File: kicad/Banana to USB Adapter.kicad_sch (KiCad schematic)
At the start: 8 parts, among them J1 USB_A, J2 Positive, J3 Negative, J4 Data

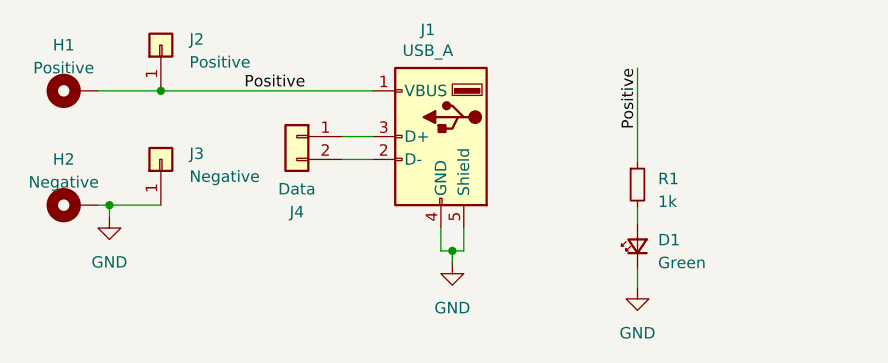
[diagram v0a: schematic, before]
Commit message: rev2 addresses #2, #3, #5, #6, #7
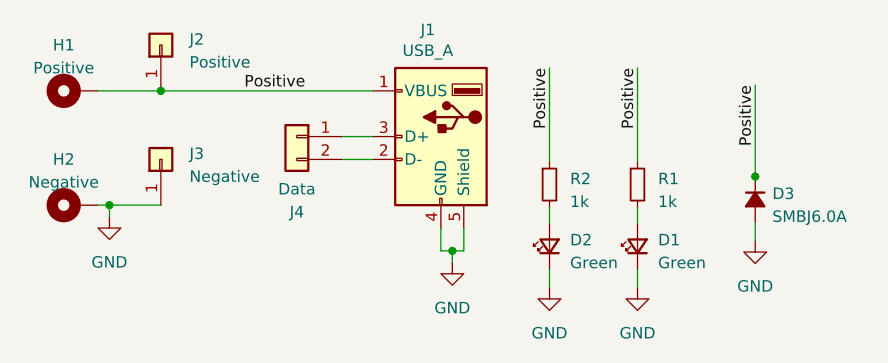
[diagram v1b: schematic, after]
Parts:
- added D2: Green, LED_SMD:LED_1206_3216Metric_Pad1.42x1.75mm_HandSolder, symbol Device:LED_Small
- added D3: SMBJ6.0A, Diode_SMD:D_SMA-SMB_Universal_Handsoldering, symbol Device:D_Small_Filled
- added R2: 1k, Resistor_SMD:R_1206_3216Metric_Pad1.30x1.75mm_HandSolder, symbol Device:R_Small
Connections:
- net GND: now also D2.1 (K), D3.2 (A)
- net Positive: now also D3.1 (K), R2.1
- new net: D2.2 (A), R2.2
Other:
- company: (none) -> baldengineer.com
- title: (none) -> Banana-to-usb adapter
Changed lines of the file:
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@@
-(kicad_sch (version 20221206) (generator eeschema)
+(kicad_sch (version 20230121) (generator eeschema)
   (paper "A4")
+  (title_block
+    (title "Banana-to-usb adapter")
+    (rev "2")
+    (company "baldengineer.com")
+  )
+  (junction (at 241.935 86.995) (diameter 0) (color 0 0 0 0)
+  )
   (junction (at 208.28 95.25) (diameter 0) (color 0 0 0 0)
   )
@@
     (stroke (width 0) (type default))
   )
+  (wire (pts (xy 241.935 76.835) (xy 241.935 86.995))
+    (stroke (width 0) (type default))
+  )
   (wire (pts (xy 168.91 77.47) (xy 175.895 77.47))
     (stroke (width 0) (type default))
@@
     (stroke (width 0) (type default))
   )
+  (wire (pts (xy 219.075 97.282) (xy 219.075 99.314))
+    (stroke (width 0) (type default))
+  )
   (wire (pts (xy 196.088 85.09) (xy 199.39 85.09))
     (stroke (width 0) (type default))
@@
     (stroke (width 0) (type default))
   )
+  (wire (pts (xy 241.935 86.995) (xy 241.935 87.249))
+    (stroke (width 0) (type default))
+  )
   (wire (pts (xy 175.895 77.47) (xy 199.39 77.47))
     (stroke (width 0) (type default))
   )
+  (wire (pts (xy 241.935 92.075) (xy 241.935 94.107))
+    (stroke (width 0) (type default))
+  )
   (wire (pts (xy 209.55 95.25) (xy 209.55 92.71))
     (stroke (width 0) (type default))
@@
   )
   (wire (pts (xy 207.01 95.25) (xy 208.28 95.25))
+    (stroke (width 0) (type default))
+  )
+  (wire (pts (xy 219.075 74.93) (xy 219.075 85.344))
+    (stroke (width 0) (type default))
+  )
+  (wire (pts (xy 219.075 90.424) (xy 219.075 92.202))
     (stroke (width 0) (type default))
   )
@@
     )
   )
+  (label "Positive" (at 219.075 74.93 270) (fields_autoplaced)
+    (effects (font (size 1.27 1.27)) (justify right bottom))
+    (property "Netclass" "Power" (at 220.345 74.93 90)
+      (effects (font (size 1.27 1.27) italic) (justify right) hide)
+    )
+  )
+  (label "Positive" (at 241.935 76.835 270) (fields_autoplaced)
+    (effects (font (size 1.27 1.27)) (justify right bottom))
+    (property "Netclass" "Power" (at 243.205 76.835 90)
+      (effects (font (size 1.27 1.27) italic) (justify right) hide)
+    )
+  )
   (symbol (lib_id "Mechanical:MountingHole_Pad") (at 166.37 90.17 90) (unit 1)
     (in_bom yes) (on_board yes) (dnp no) (fields_autoplaced)
@@
         (path "/b8d30d27-a840-4da1-9b57-1f9fe5fa1469"
           (reference "#PWR02") (unit 1)
+        )
+      )
+    )
+  )
+  (symbol (lib_id "Device:LED_Small") (at 219.075 94.742 90) (unit 1)
+    (in_bom yes) (on_board yes) (dnp no) (fields_autoplaced)
+    (property "Reference" "D2" (at 221.361 94.0435 90)
+      (effects (font (size 1.27 1.27)) (justify right))
+    )
+    (property "Value" "Green" (at 221.361 96.5835 90)
+      (effects (font (size 1.27 1.27)) (justify right))
+    )
+    (property "Footprint" "LED_SMD:LED_1206_3216Metric_Pad1.42x1.75mm_HandSolder" (at 219.075 94.742 90)
+      (effects (font (size 1.27 1.27)) hide)
+    )
+    (property "Datasheet" "~" (at 219.075 94.742 90)
+      (effects (font (size 1.27 1.27)) hide)
+    )
+    (pin "1")
+    (pin "2")
+    (instances
+      (project "Banana to USB Adapter"
+        (path "/b8d30d27-a840-4da1-9b57-1f9fe5fa1469"
+          (reference "D2") (unit 1)
         )
       )
@@
     )
   )
+  (symbol (lib_id "power:GND") (at 219.075 99.314 0) (unit 1)
+    (in_bom yes) (on_board yes) (dnp no) (fields_autoplaced)
+    (property "Reference" "#PWR05" (at 219.075 105.664 0)
+      (effects (font (size 1.27 1.27)) hide)
+    )
+    (property "Value" "GND" (at 219.075 104.394 0)
+      (effects (font (size 1.27 1.27)))
+    )
+    (property "Footprint" "" (at 219.075 99.314 0)
+      (effects (font (size 1.27 1.27)) hide)
+    )
+    (property "Datasheet" "" (at 219.075 99.314 0)
+      (effects (font (size 1.27 1.27)) hide)
+    )
+    (pin "1")
+    (instances
+      (project "Banana to USB Adapter"
+        (path "/b8d30d27-a840-4da1-9b57-1f9fe5fa1469"
+          (reference "#PWR05") (unit 1)
+        )
+      )
+    )
+  )
   (symbol (lib_id "Connector_Generic:Conn_01x01") (at 175.895 85.09 90) (unit 1)
     (in_bom yes) (on_board yes) (dnp no) (fields_autoplaced)
@@
         (path "/b8d30d27-a840-4da1-9b57-1f9fe5fa1469"
           (reference "J3") (unit 1)
+        )
+      )
+    )
+  )
+  (symbol (lib_id "Device:D_Small_Filled") (at 241.935 89.535 270) (unit 1)
+    (in_bom yes) (on_board yes) (dnp no) (fields_autoplaced)
+    (property "Reference" "D3" (at 243.84 88.9 90)
+      (effects (font (size 1.27 1.27)) (justify left))
+    )
+    (property "Value" "SMBJ6.0A" (at 243.84 91.44 90)
+      (effects (font (size 1.27 1.27)) (justify left))
+    )
+    (property "Footprint" "Diode_SMD:D_SMA-SMB_Universal_Handsoldering" (at 241.935 89.535 90)
+      (effects (font (size 1.27 1.27)) hide)
+    )
+    (property "Datasheet" "https://www.farnell.com/datasheets/1874873.pdf" (at 241.935 89.535 90)
+      (effects (font (size 1.27 1.27)) hide)
+    )
+    (property "Sim.Device" "D" (at 241.935 89.535 0)
+      (effects (font (size 1.27 1.27)) hide)
+    )
+    (property "Sim.Pins" "1=K 2=A" (at 241.935 89.535 0)
+      (effects (font (size 1.27 1.27)) hide)
+    )
+    (pin "1")
+    (pin "2")
+    (instances
+      (project "Banana to USB Adapter"
+        (path "/b8d30d27-a840-4da1-9b57-1f9fe5fa1469"
+          (reference "D3") (unit 1)
         )
       )
@@
         )
       )
+    )
+  )
+  (symbol (lib_id "power:GND") (at 241.935 94.107 0) (unit 1)
+    (in_bom yes) (on_board yes) (dnp no) (fields_autoplaced)
+    (property "Reference" "#PWR04" (at 241.935 100.457 0)
+      (effects (font (size 1.27 1.27)) hide)
+    )
+    (property "Value" "GND" (at 241.935 99.187 0)
+      (effects (font (size 1.27 1.27)))
+    )
+    (property "Footprint" "" (at 241.935 94.107 0)
+      (effects (font (size 1.27 1.27)) hide)
+    )
+    (property "Datasheet" "" (at 241.935 94.107 0)
+      (effects (font (size 1.27 1.27)) hide)
+    )
+    (pin "1")
+    (instances
+      (project "Banana to USB Adapter"
+        (path "/b8d30d27-a840-4da1-9b57-1f9fe5fa1469"
+          (reference "#PWR04") (unit 1)
+        )
+      )
+    )
+  )
+  (symbol (lib_id "Device:R_Small") (at 219.075 87.884 0) (unit 1)
+    (in_bom yes) (on_board yes) (dnp no) (fields_autoplaced)
+    (property "Reference" "R2" (at 221.361 87.249 0)
+      (effects (font (size 1.27 1.27)) (justify left))
+    )
+    (property "Value" "1k" (at 221.361 89.789 0)
+      (effects (font (size 1.27 1.27)) (justify left))
+    )
+    (property "Footprint" "Resistor_SMD:R_1206_3216Metric_Pad1.30x1.75mm_HandSolder" (at 219.075 87.884 0)
+      (effects (font (size 1.27 1.27)) hide)
+    )
+    (property "Datasheet" "~" (at 219.075 87.884 0)
+      (effects (font (size 1.27 1.27)) hide)
+    )
+    (pin "1")
+    (pin "2")
+    (instances
+      (project "Banana to USB Adapter"
+        (path "/b8d30d27-a840-4da1-9b57-1f9fe5fa1469"
+          (reference "R2") (unit 1)
+        )
+      )
